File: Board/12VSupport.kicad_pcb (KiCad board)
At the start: 2 copper layers, 106.7 x 123.2 mm, 73 parts, among them J1 12V, J2 BATT, J3 BUCK_IN, J4 BUCK_OUT, J5 BOOST_IN, J6 BOOST_OUT, J7 TMP36GZ, J8 HEATER, J9 ICSP, K1 SLA-05VDC-SL-C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

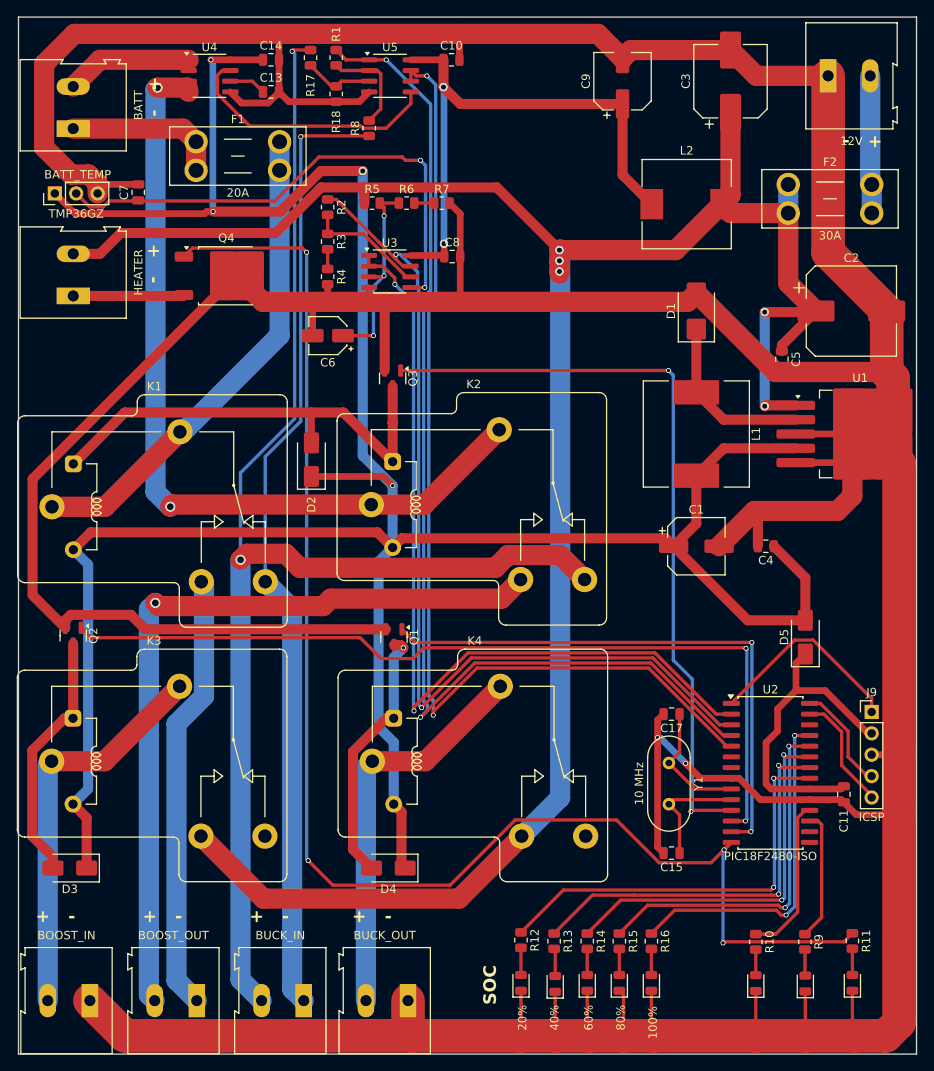
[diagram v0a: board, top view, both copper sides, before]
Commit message: Change fuse holders.
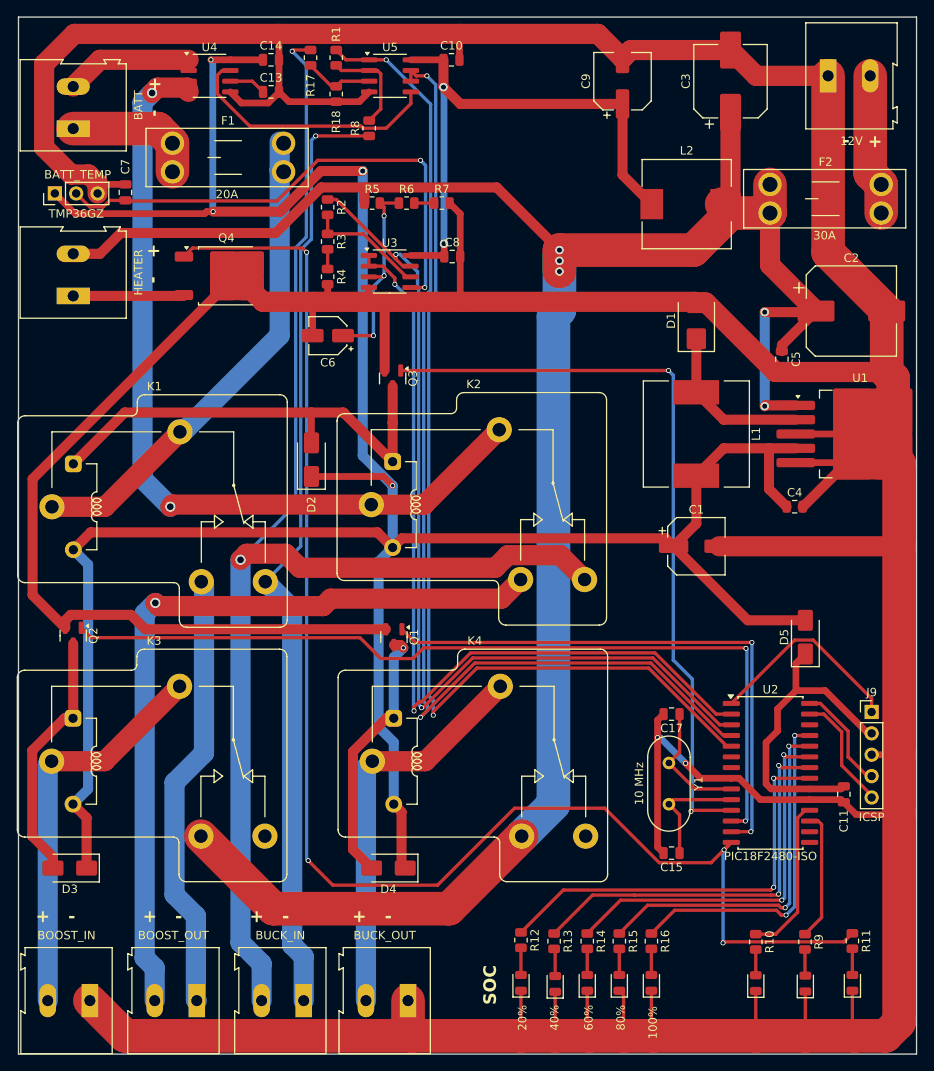
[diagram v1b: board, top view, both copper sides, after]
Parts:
- F1, F2: footprint Fuse:Fuseholder_Blade_Mini_Keystone_3568 -> spetry:Fuseholder_Blade
- moved C4 5.81 mm to (134.1, 100.1), turned to 0 degrees
- moved F1 2.82 mm to (60.2, 56.9)
- moved F2 2.17 mm to (131.2, 61.8)
- moved C7 1.52 mm to (54.6, 62.7)
- moved D1 1.14 mm to (122.4, 78.0)
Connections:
- net /MCU/VPP_~{MCLR} renamed /MCU/VPP
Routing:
- net /BAT-: track 18.6 -> 15.9 mm
- net VCC: track 326.3 -> 323.8 mm
- net Net-(K2-Pad11A): track 97.6 -> 98.9 mm
- net REL_HEATER: track 173.5 -> 174.7 mm
- net BUCK+: track 162.5 -> 163.7 mm
- net Net-(D1-K): track 20.7 -> 19.5 mm
- net BUCK-: track 114.4 -> 113.4 mm

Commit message: Fixes current sensor
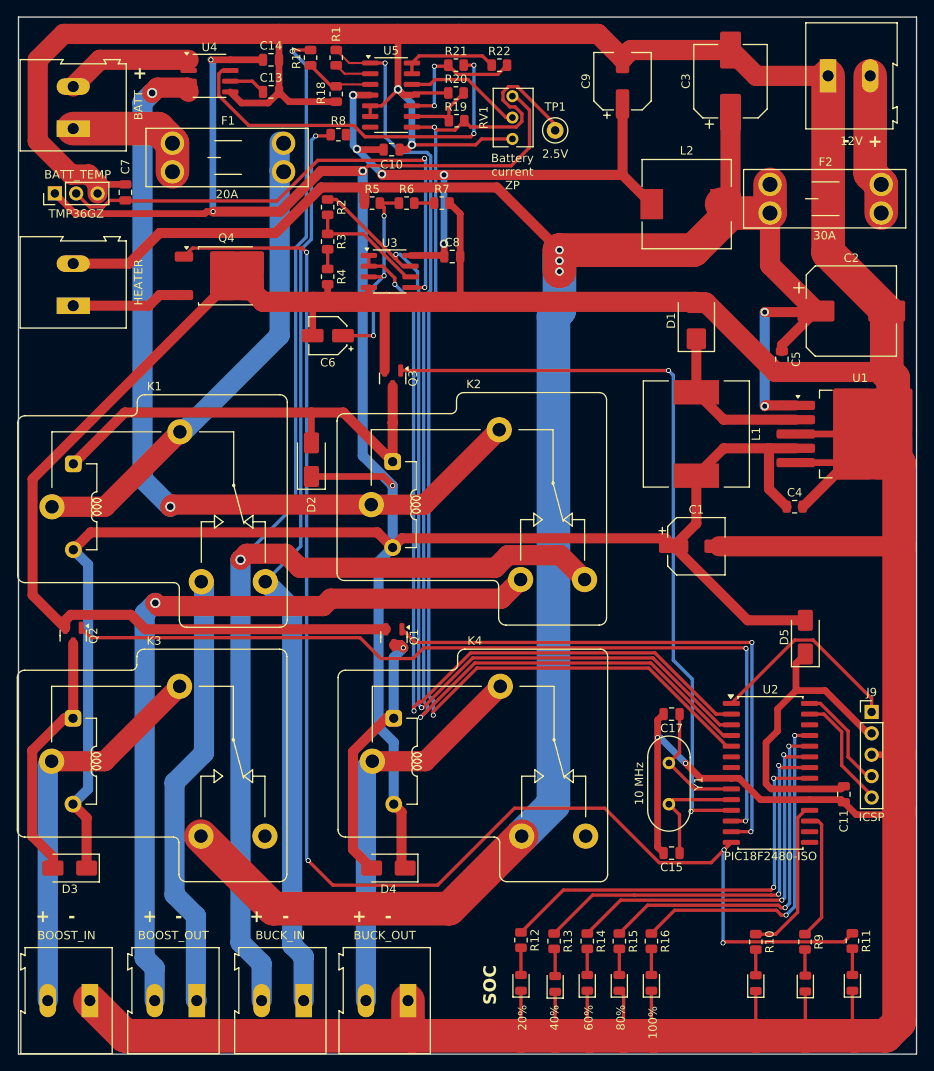
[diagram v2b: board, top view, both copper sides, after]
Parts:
- added R19: 10K, Resistor_SMD:R_0805_2012Metric, F.Cu at (94.0, 54.2)
- added R20: 10K, Resistor_SMD:R_0805_2012Metric, F.Cu at (93.9, 50.9)
- added R21: 10K, Resistor_SMD:R_0805_2012Metric, F.Cu at (93.9, 47.6)
- added R22: 10K, Resistor_SMD:R_0805_2012Metric, F.Cu at (99.0, 47.6)
- added RV1: 10K, Potentiometer_THT:Potentiometer_Bourns_3266Y_Vertical, F.Cu at (100.6, 51.3)
- added TP1: 2.5V, TestPoint:TestPoint_Loop_D1.80mm_Drill1.0mm_Beaded, F.Cu at (105.7, 55.4)
- U5: value LM358 -> LM324; footprint Package_SO:SOIC-8_3.9x4.9mm_P1.27mm -> Package_SO:SOIC-14_3.9x8.7mm_P1.27mm
- moved C10 12.8 mm to (86.2, 57.7)
- moved R8 3.74 mm to (79.9, 55.9), turned to 0 degrees
- moved U5 2.29 mm to (86.2, 51.2)
- moved J8 1.17 mm to (48.4, 76.2)
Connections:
- U5 pad 4: GND -> /Sensors/V+_OP
- U5 pad 5: BAT_CURR -> GND
- U5 pad 6: CURR_SENSE -> GND
- U5 pad 7: CURR_SENSE -> unconnected-(U5-Pad7)
- U5 pad 8: /Sensors/V+_OP -> CURR_SENSE
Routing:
- net GND: track 710.5 -> 743.9 mm, vias 2 -> 4
- net VCC: track 323.8 -> 351.9 mm
- net CURR_SENSE: track 122.2 -> 140.3 mm
- net Net-(U5C-+): track 0.00 -> 17.0 mm, vias 0 -> 2
- net BAT_CURR: track 31.3 -> 46.0 mm, vias 0 -> 2
- net Net-(U5D-+): track 0.00 -> 14.1 mm
- net /Sensors/VCC/2: track 0.00 -> 11.6 mm
- net Net-(U5C--): track 0.00 -> 8.63 mm
- net Net-(U5A--): track 11.8 -> 4.45 mm
- net /Sensors/V+_OP: track 66.8 -> 71.8 mm, vias 2 -> 5
- net BUCK-: track 113.4 -> 108.9 mm
- net BAT_SENSE: track 130.8 -> 132.3 mm
- net Net-(J7-Pin_2): track 61.0 -> 61.6 mm
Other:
- board text added: "+"
- board text added: "Battery current ZP"

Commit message: Remove diode in MCU supply line so MCU has full 5V.
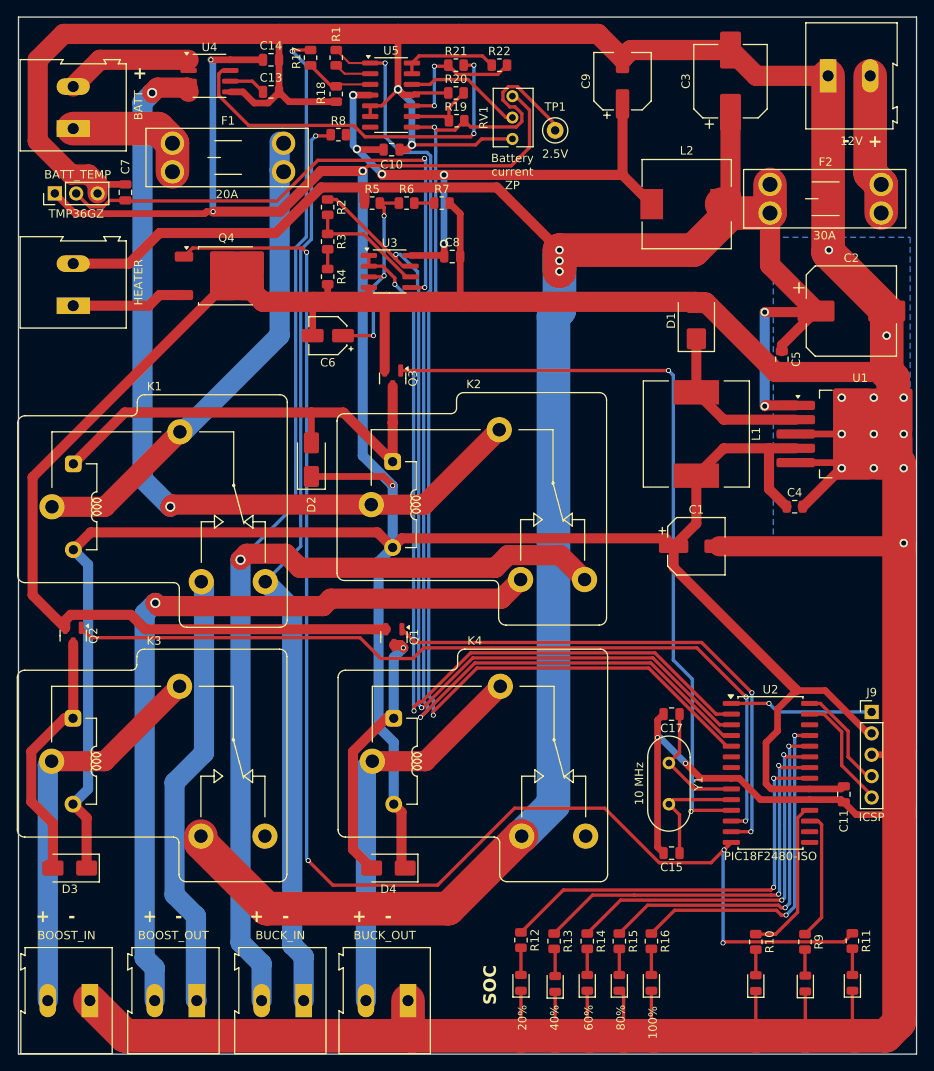
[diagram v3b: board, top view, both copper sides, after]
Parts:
- removed D5: SS14, Diode_SMD:D_SMA
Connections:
- C11 pad 1: /MCU/VCC_PIC -> VCC
- J9 pad 2: /MCU/VCC_PIC -> VCC
- U2 pad 20: /MCU/VCC_PIC -> VCC
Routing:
- net /MCU/VCC_PIC: track 38.1 -> 0.00 mm
- net VCC: track 351.9 -> 389.1 mm
- net /MCU/VPP: track 24.3 -> 17.1 mm, vias 0 -> 1
- net REL_BUCK_OUT: track 67.1 -> 63.6 mm
- net REL_BOOST_IN: track 103.3 -> 100.0 mm
- net GND: track 743.9 -> 744.1 mm, vias 4 -> 16
- added copper zone on B.Cu, net GND

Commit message: Added ground plane.
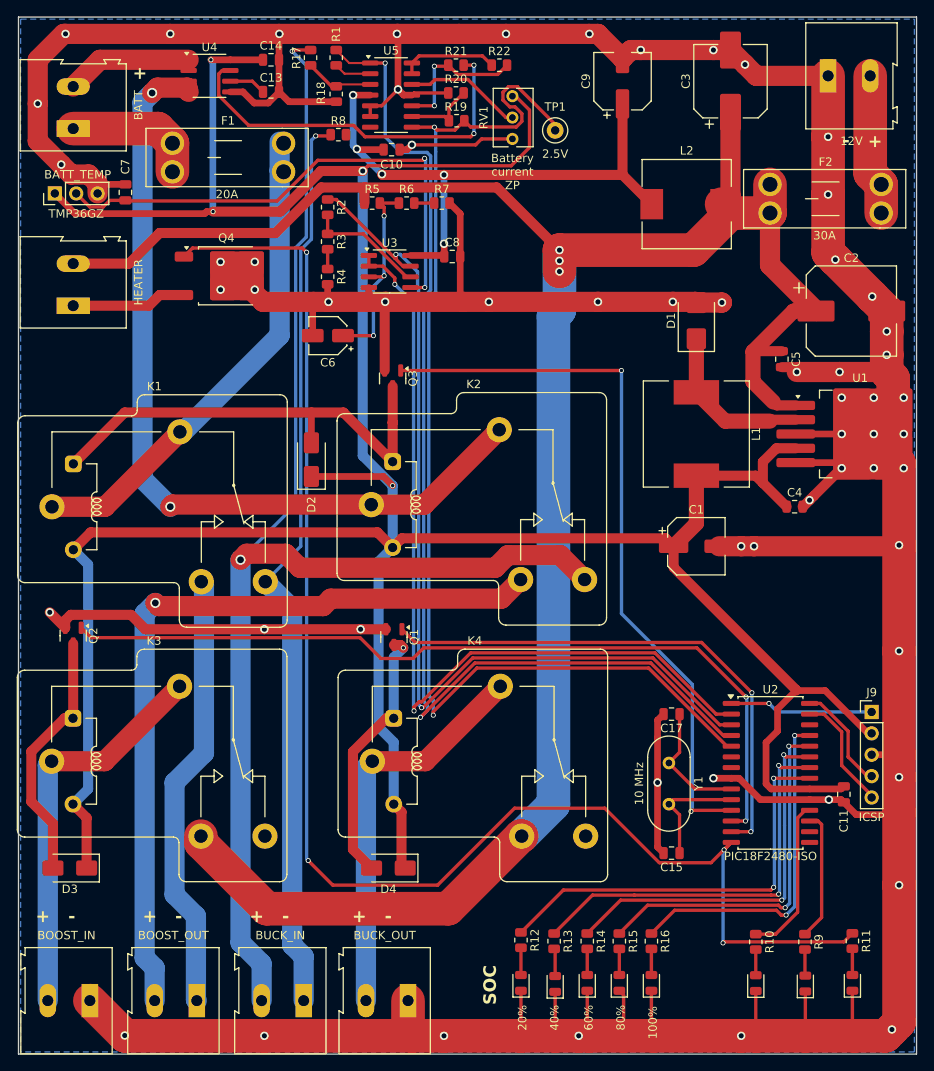
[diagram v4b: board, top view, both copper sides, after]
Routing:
- net GND: track 744.1 -> 669.1 mm, vias 16 -> 59
- net +12V: track 270.7 -> 266.1 mm, vias 5 -> 3
- net REL_CHARGE: track 90.3 -> 87.0 mm
- net VCC: track 389.1 -> 387.4 mm

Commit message: Board WIP
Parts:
- added C12: 100u, Capacitor_THT:CP_Radial_D6.3mm_P2.50mm, F.Cu at (134.5, 112.8)
- added L3: 3u, spetry:CD43, F.Cu at (127.5, 112.8)
- added REF**: MountingHole_3.2mm_M3_Pad_Via, MountingHole:MountingHole_3.2mm_M3_Pad_Via, F.Cu at (46.7, 144.8)
- added REF**: MountingHole_3.2mm_M3_Pad_Via, MountingHole:MountingHole_3.2mm_M3_Pad_Via, F.Cu at (143.9, 46.4)
- added REF**: MountingHole_3.2mm_M3_Pad_Via, MountingHole:MountingHole_3.2mm_M3_Pad_Via, F.Cu at (46.9, 83.9)
- added REF**: MountingHole_3.2mm_M3_Pad_Via, MountingHole:MountingHole_3.2mm_M3_Pad_Via, F.Cu at (143.9, 160.4)
- C6: footprint Capacitor_SMD:CP_Elec_4x5.4 -> Capacitor_SMD:C_1206_3216Metric_Pad1.33x1.80mm_HandSolder
- F2: value 30A -> 40A
- moved D8 17.3 mm to (123.7, 156.6)
- moved R11 17.3 mm to (123.7, 151.7)
- moved J1 7.75 mm to (130.3, 48.9)
- moved D3 7.37 mm to (55.4, 143.0)
- moved C3 5.73 mm to (120.9, 50.8)
- moved C9 2.93 mm to (110.7, 49.8)
- moved D6 2.54 mm to (132.8, 156.7)
- moved R9 2.54 mm to (132.8, 151.8)
- moved D7 1.27 mm to (128.2, 156.7)
- moved R10 1.27 mm to (128.2, 151.8)
- moved C6 0.08 mm to (78.7, 79.8)
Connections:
- C11 pad 1: VCC -> /MCU/VCC_PIC
- J9 pad 2: VCC -> /MCU/VCC_PIC
- U2 pad 20: VCC -> /MCU/VCC_PIC
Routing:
- net GND: track 669.1 -> 617.3 mm, vias 59 -> 55
- net /MCU/VCC_PIC: track 0.00 -> 47.8 mm
- net VCC: track 387.4 -> 345.4 mm
- net Net-(U5A--): track 4.45 -> 14.8 mm, vias 0 -> 2
- net REL_HEATER: track 174.7 -> 169.2 mm, vias 4 -> 2
- net Net-(J5-Pin_2): track 47.5 -> 52.5 mm
- net Net-(D3-A): track 30.4 -> 34.2 mm
- net Net-(J1-Pin_2): track 16.8 -> 20.1 mm
- net /BAT+: track 15.0 -> 17.7 mm, vias 0 -> 2
- net Net-(U2-TX/CK/RC6): track 15.4 -> 18.0 mm
- net BUCK+: track 163.7 -> 166.0 mm
- net +12V: track 266.1 -> 267.8 mm
- net Net-(U2-RX/DT/RC7): track 19.1 -> 20.3 mm
- net Net-(U2-RB4/KBI0/AN9): track 40.9 -> 39.8 mm
- net /Sensors/V+_OP: track 71.8 -> 72.7 mm
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
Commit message: Rev 1.0
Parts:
- added R23: 22K, Resistor_SMD:R_0805_2012Metric, F.Cu at (129.5, 118.1)
- added REF**: ESD-Logo_8.9x8mm_SilkScreen, Symbol:ESD-Logo_8.9x8mm_SilkScreen, F.Cu at (143.0, 145.8)
- added REF**: OSHW-Logo_7.5x8mm_SilkScreen, Symbol:OSHW-Logo_7.5x8mm_SilkScreen, F.Cu at (101.6, 70.4)
- moved J9 5.07 mm to (143.3, 119.4)
- moved J5 2.49 mm to (52.9, 158.8)
- moved J3 2.49 mm to (78.3, 158.8)
- moved J4 2.49 mm to (90.7, 158.8)
- moved J6 2.49 mm to (65.6, 158.8)
- moved D1 1.77 mm to (124.2, 78.0)
- moved C15 0.84 mm to (119.1, 140.5)
- moved C17 0.84 mm to (119.1, 125.5)
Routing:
- net /MCU/PGC: track 13.9 -> 9.37 mm
- net /MCU/VPP: track 17.1 -> 21.6 mm, vias 1 -> 0
- net /MCU/VCC_PIC: track 47.8 -> 51.4 mm, vias 0 -> 1
- net /MCU/PGD: track 12.7 -> 9.28 mm
- net GND: track 617.3 -> 615.6 mm
- net BUCK-: track 108.9 -> 110.0 mm
- net BUCK+: track 166.0 -> 167.0 mm
- net Net-(J5-Pin_2): track 52.5 -> 51.4 mm
- net Net-(J4-Pin_2): track 47.6 -> 48.7 mm
- net Net-(J6-Pin_1): track 52.4 -> 53.5 mm
- net Net-(J6-Pin_2): track 93.1 -> 94.2 mm
- net Net-(D1-K): track 19.7 -> 20.4 mm
- net /MCU/OSC1: track 15.0 -> 14.4 mm
- net /MCU/OSC2: track 14.0 -> 13.4 mm
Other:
- rule pad_to_mask_clearance: 0.05 -> 0
- board text added: "Rev. 1.0 2024"
- board text added: "github.com/svpetry/12VSupport"
